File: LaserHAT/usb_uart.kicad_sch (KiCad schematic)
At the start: 9 parts

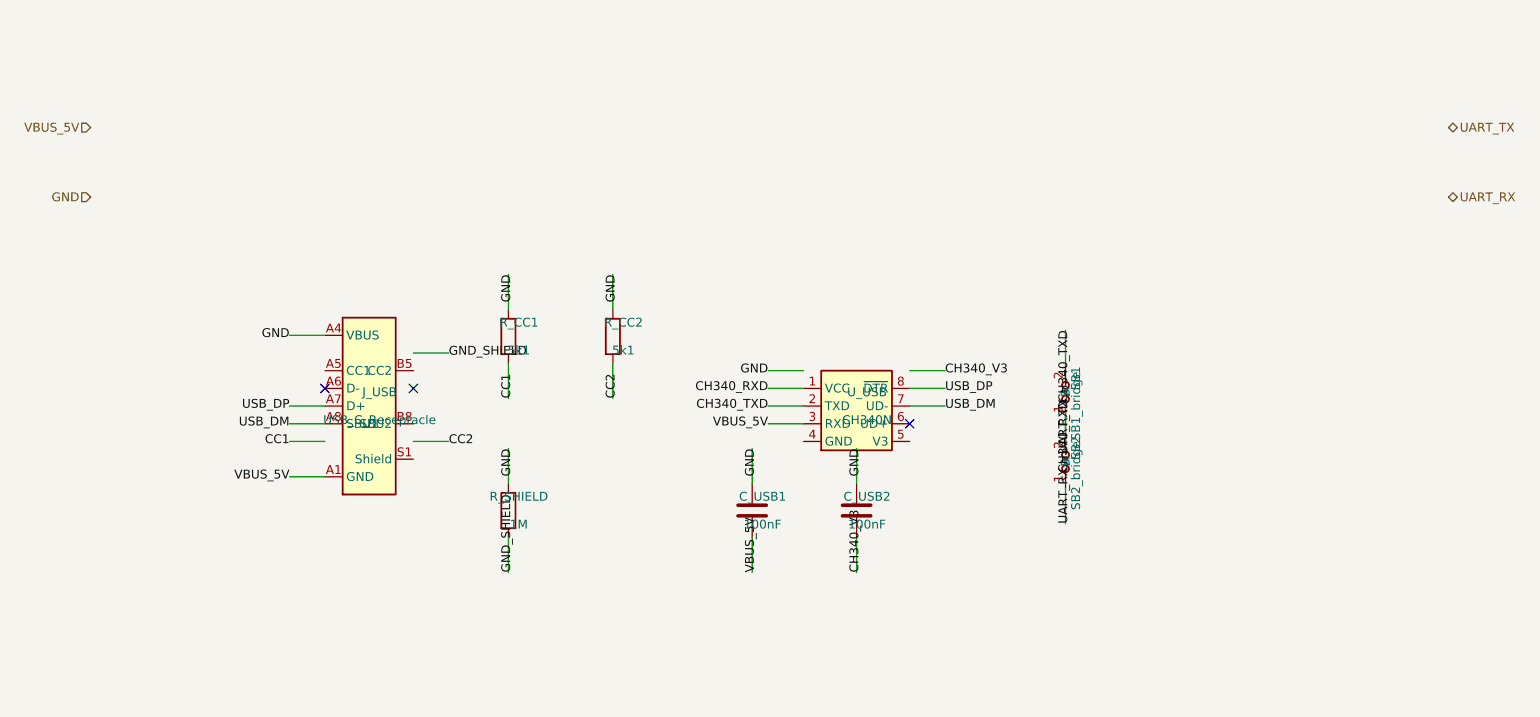
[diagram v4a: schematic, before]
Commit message: Fix floating hierarchical_labels in child schematics
Every hierarchical_label must be at the end of a connected wire stub.
The generated schematics had hlabels placed at sheet-edge coordinates
(5,20-80) and (200,20-50) with no wires, while using local labels at
the actual pin stubs.

fix_labels.py:
- Removes floating hlabels from mspm0_controller and usb_uart sheets
- Replaces each signal's local label with a hierarchical_label at the
  same wire-stub position (9 signals in MSPM0, 4 in USB-UART)
- Adds VCC_3V3_MCU/GND hlabels in MSPM0 via short wire stubs branching
  off the existing VDD/VSS power symbol connection points

Also commits generate_schematics.py verbatim-injection patch and minor
wire UUID refresh in laser_driver_circuit.kicad_sch.

Co-Authored-By: Claude Sonnet 4.6 <noreply@anthropic.com>
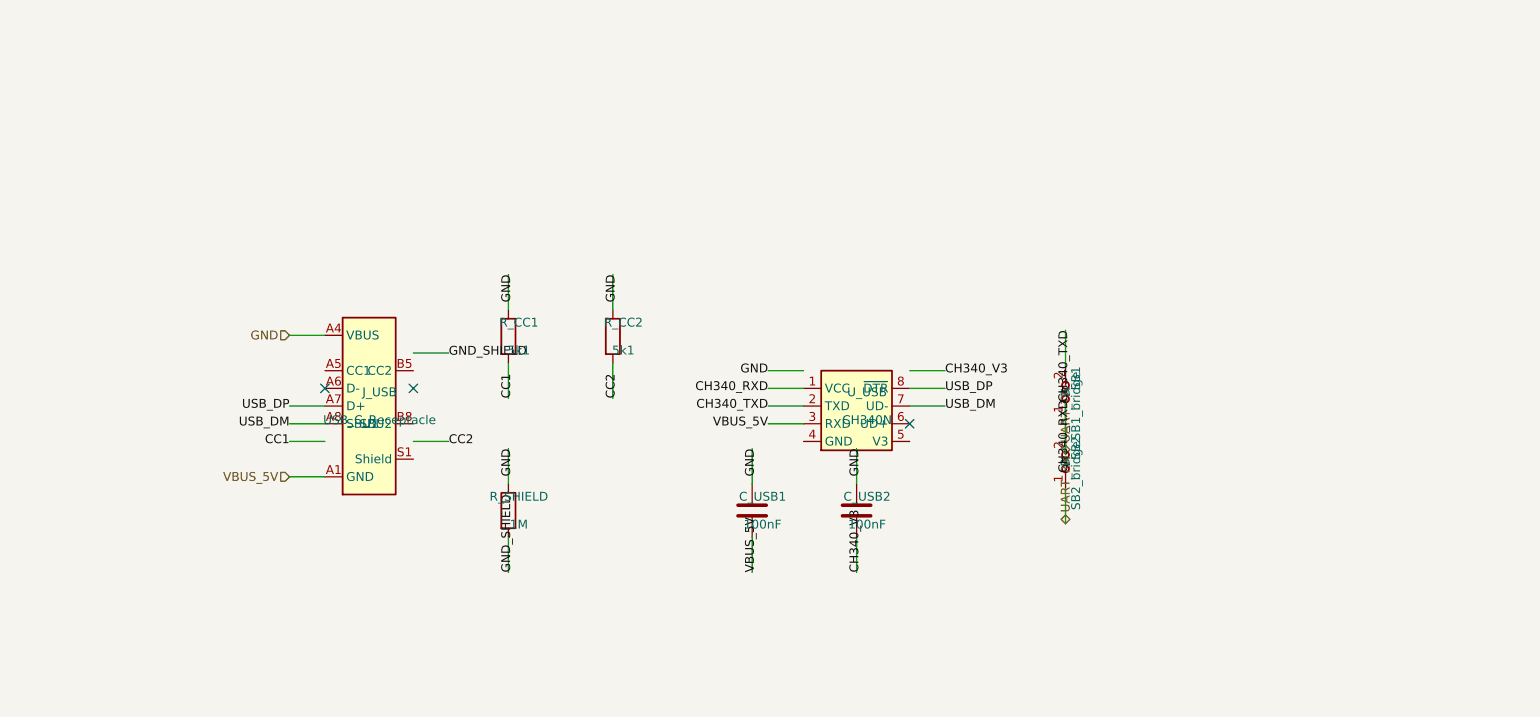
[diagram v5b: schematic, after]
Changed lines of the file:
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@@
     (stroke (width 0) (type default))
   )
-  (label "VBUS_5V" (at 33.57 70.16 180)
+  (hierarchical_label "VBUS_5V" (shape input) (at 33.57 70.16 180)
     (effects (font (size 1.27 1.27)))
   )
@@
     (effects (font (size 1.27 1.27)))
   )
-  (label "GND" (at 33.57 49.84 180)
+  (hierarchical_label "GND" (shape input) (at 33.57 49.84 180)
     (effects (font (size 1.27 1.27)))
   )
@@
     (effects (font (size 1.27 1.27)))
   )
-  (label "UART_TX" (at 145.0 66.89 90)
+  (hierarchical_label "UART_TX" (shape bidirectional) (at 145.0 66.89 90)
     (effects (font (size 1.27 1.27)))
   )
@@
     (effects (font (size 1.27 1.27)))
   )
-  (label "UART_RX" (at 145.0 76.89 90)
-    (effects (font (size 1.27 1.27)))
-  )
-  (hierarchical_label "VBUS_5V" (shape input) (at 5 20 180)
-    (effects (font (size 1.27 1.27)))
-  )
-  (hierarchical_label "GND" (shape input) (at 5 30 180)
-    (effects (font (size 1.27 1.27)))
-  )
-  (hierarchical_label "UART_TX" (shape bidirectional) (at 200 20 0)
-    (effects (font (size 1.27 1.27)))
-  )
-  (hierarchical_label "UART_RX" (shape bidirectional) (at 200 30 0)
+  (hierarchical_label "UART_RX" (shape bidirectional) (at 145.0 76.89 90)
     (effects (font (size 1.27 1.27)))
   )
@@
   )
   (symbol_instances
-    (path "/212bfd25-f831-4b85-926b-000000000004/50dc2b85-6e56-463d-938c-c9b5e5251356"
+    (path "/212bfd25-f831-4b85-926b-000000000004/c849b868-bf8b-46cc-9b71-629852d0a3f0"
       (reference "J_USB") (unit 1) (value "USB_C_Receptacle") (footprint "Connector_USB:USB_C_Receptacle_GCT_USB4125")
     )
-    (path "/212bfd25-f831-4b85-926b-000000000004/e9dbbd6a-570c-4209-82c4-f676de474bc6"
+    (path "/212bfd25-f831-4b85-926b-000000000004/08e6c995-b1bc-4d7e-9743-164015a89f2f"
       (reference "R_CC1") (unit 1) (value "5k1") (footprint "Resistor_SMD:R_0402_1005Metric")
     )
-    (path "/212bfd25-f831-4b85-926b-000000000004/c97010d5-b40c-4a1b-8ab2-49e8ee4077aa"
+    (path "/212bfd25-f831-4b85-926b-000000000004/063f2b16-9f71-4130-bd8d-94e3bcb002a7"
       (reference "R_CC2") (unit 1) (value "5k1") (footprint "Resistor_SMD:R_0402_1005Metric")
     )
-    (path "/212bfd25-f831-4b85-926b-000000000004/6643c6db-d436-464e-85c8-bcf5f708e534"
+    (path "/212bfd25-f831-4b85-926b-000000000004/e2719e88-67af-4952-88f8-6ae716037459"
       (reference "R_SHIELD") (unit 1) (value "1M") (footprint "Resistor_SMD:R_0402_1005Metric")
     )
-    (path "/212bfd25-f831-4b85-926b-000000000004/22bd5166-6294-4ac8-9ad9-a0bc21f87446"
+    (path "/212bfd25-f831-4b85-926b-000000000004/1ccfa51b-02f7-4dfb-b4b6-7f130c770bd6"
       (reference "U_USB") (unit 1) (value "CH340N") (footprint "Package_SO:SOIC-8_3.9x4.9mm_P1.27mm")
     )
-    (path "/212bfd25-f831-4b85-926b-000000000004/00e72fd9-97d5-4396-965a-ede833e229ab"
+    (path "/212bfd25-f831-4b85-926b-000000000004/c104b3dd-97b8-4380-bd4b-b54e92deff57"
       (reference "C_USB1") (unit 1) (value "100nF") (footprint "Capacitor_SMD:C_0402_1005Metric")
     )
-    (path "/212bfd25-f831-4b85-926b-000000000004/3160f2aa-1f47-47c4-9b02-5ceb3f61dff5"
+    (path "/212bfd25-f831-4b85-926b-000000000004/101264b4-3f90-4856-97e8-1900abaeb8fe"
       (reference "C_USB2") (unit 1) (value "100nF") (footprint "Capacitor_SMD:C_0402_1005Metric")
     )
-    (path "/212bfd25-f831-4b85-926b-000000000004/15e7e694-8d0e-4f92-ae43-5f42842a6977"
+    (path "/212bfd25-f831-4b85-926b-000000000004/eee1abfc-00af-4930-8bdc-0be285381b33"
       (reference "SB1") (unit 1) (value "SB1_bridge") (footprint "Jumper:SolderJumper-2_P1.3mm_Open_RoundedPad1.0x1.5mm")
     )
-    (path "/212bfd25-f831-4b85-926b-000000000004/41149967-97ff-45bb-99a2-b8a2602378f4"
+    (path "/212bfd25-f831-4b85-926b-000000000004/53f376c3-f1e7-4674-9a7b-776828c63edd"
       (reference "SB2") (unit 1) (value "SB2_bridge") (footprint "Jumper:SolderJumper-2_P1.3mm_Open_RoundedPad1.0x1.5mm")
     )
